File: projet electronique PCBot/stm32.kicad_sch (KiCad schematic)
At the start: 6 parts, among them J1 Conn_ST_STDC14, U1 STM32G431KBT6

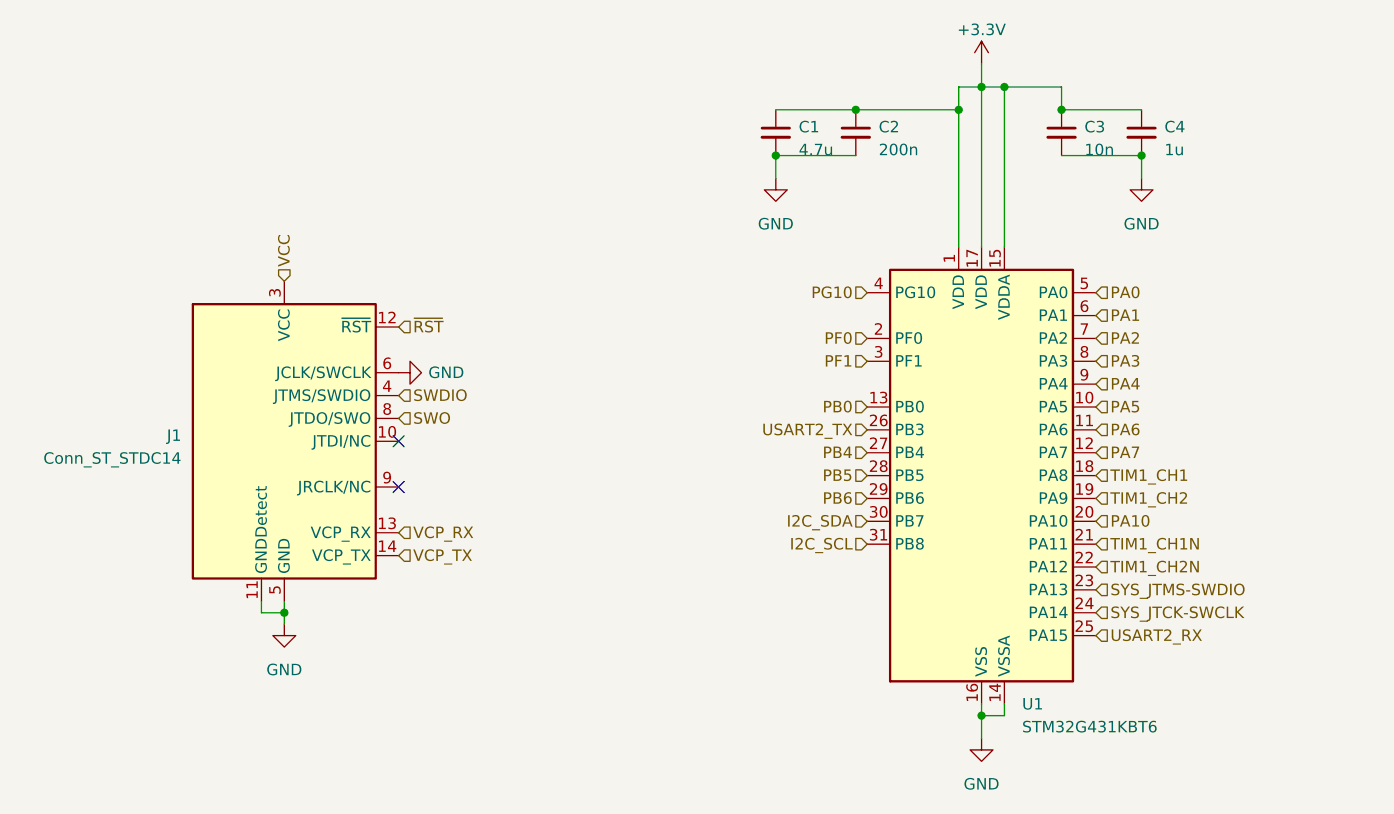
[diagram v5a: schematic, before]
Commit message: ajout de connexions
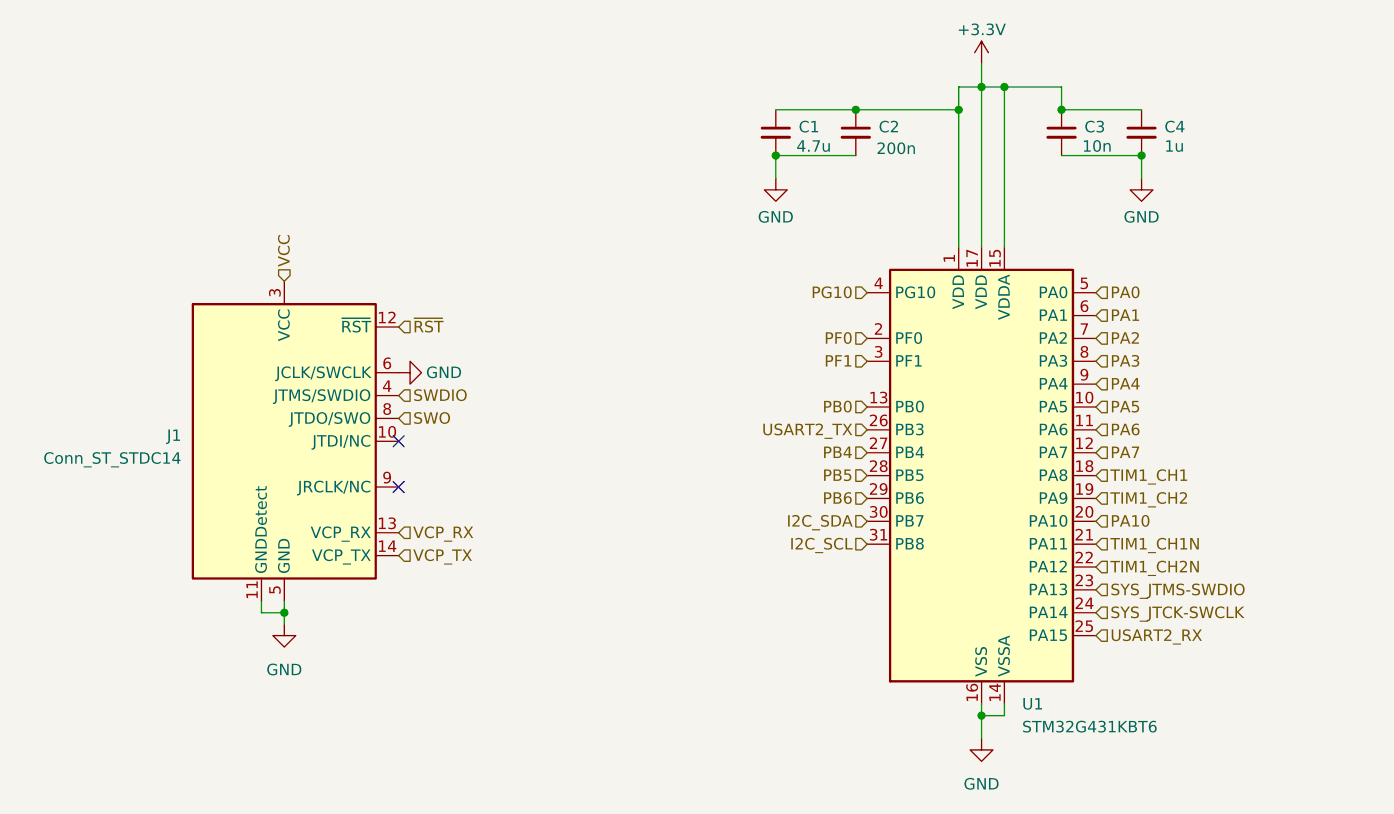
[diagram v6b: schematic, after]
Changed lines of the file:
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@@
 		(on_board yes)
 		(dnp no)
-		(fields_autoplaced yes)
 		(property "Reference" "C2"
 			(at 133.35 67.9513 0)
@@
 		)
 		(property "Value" "200n"
-			(at 133.35 70.4913 0)
+			(at 133.096 70.358 0)
 			(effects
 				(font
@@
 		)
 		(property "Value" "10n"
-			(at 156.21 70.4913 0)
+			(at 155.956 70.104 0)
 			(effects
 				(font
@@
 		(on_board yes)
 		(dnp no)
-		(fields_autoplaced yes)
 		(property "Reference" "#PWR04"
 			(at 121.92 80.01 0)
@@
 		)
 		(property "Value" "GND"
-			(at 121.92 78.74 0)
+			(at 121.92 77.978 0)
 			(effects
 				(font
@@
 		)
 		(property "Value" "GND"
-			(at 83.312 95.25 90)
+			(at 83.058 95.25 90)
 			(effects
 				(font
@@
 		)
 		(property "Value" "4.7u"
-			(at 124.46 70.4913 0)
+			(at 124.206 70.104 0)
 			(effects
 				(font
@@
 		(on_board yes)
 		(dnp no)
-		(fields_autoplaced yes)
 		(property "Reference" "C4"
 			(at 165.1 67.9513 0)
@@
 		)
 		(property "Value" "1u"
-			(at 165.1 70.4913 0)
+			(at 165.1 70.104 0)
 			(effects
 				(font
@@
 		(on_board yes)
 		(dnp no)
-		(fields_autoplaced yes)
 		(property "Reference" "#PWR011"
 			(at 162.56 80.01 0)
@@
 		)
 		(property "Value" "GND"
-			(at 162.56 78.74 0)
-			(effects
-				(font
+			(at 162.56 77.978 0)
+			(effects
+				(font

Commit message: modifs
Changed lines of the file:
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@@
 		(on_board yes)
 		(dnp no)
-		(fields_autoplaced yes)
 		(property "Reference" "#PWR015"
 			(at 67.31 129.54 0)
@@
 		)
 		(property "Value" "GND"
-			(at 67.31 128.27 0)
+			(at 67.31 127.508 0)
 			(effects
 				(font

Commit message: re modif de lundi
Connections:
- net SWDIO is gone; now on net SYS_JTMS-SWDIO: J1.4 (JTMS/SWDIO)
- net SWO is gone; now on net USART2_TX: J1.8 (JTDO/SWO)
- net VCC is gone; now on net +3.3V: J1.3 (VCC)
- net VCP_RX is gone; now on net USART2_TX: J1.13 (VCP_RX)
- net VCP_TX is gone; now on net USART2_RX: J1.14 (VCP_TX)
- net GND: no longer J1.6 (JCLK/SWCLK)
- net SYS_JTCK-SWCLK: now also J1.6 (JCLK/SWCLK)
- net ~{RST} renamed NRST
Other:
- note added: "NRST????"
- moved on the sheet: C3, C4
